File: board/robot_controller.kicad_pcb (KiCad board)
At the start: 2 copper layers, 325 parts, among them J101 +3.3V, J102 +24V, J103 GND, J104 JTAG-ARM, J105 Power, J106 FTDI-USB, J107 Industrial Inputs, J108 Industrial Outputs, J109 MCU-USB, J110 AUX-UART, J111 UEXT0, J112 UEXT1, J113 RGB LEDs, J201 Temp Probe, J2301 Stepper Motor, J2302 Limit-SW, J2401 Stepper Motor, J2402 Limit-SW, J2501 Stepper Motor, J2502 Limit-SW, J2601 Stepper Motor, J2602 Limit-SW, J301 Temp Probe, Q101 PNP, Q1501 NJT4031NT1G, Q1601 NJT4031NT1G, Q1701 NJT4031NT1G, Q1801 NJT4031NT1G, Q1901 NJT4031NT1G, Q2001 NJT4031NT1G, Q2101 NJT4031NT1G, Q2201 NJT4031NT1G, Q401 MMBT5962, Q402 MMBT5962, Q501 MMBT5962, Q502 MMBT5962, SW101 SW0, SW102 SW1, SW103 SW2, SW104 SW3, SW105 RESET, SW106 BOOT, U101 STM32F405-144, U102 FT232RL, U201 MAX6675, U2301 L6470, U2401 L6470, U2501 L6470, U2601 L6470, U301 MAX6675, U601 LMZ14201, X101 8MHZ

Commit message: Board pretty much done.
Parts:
- added G***: LOGO, components:roboteurs, F.Cu at (123.2, -139.1)
- added G***: LOGO, components:hypertriangle, F.Cu at (95.6, -139.1)
- added G***: LOGO, components:resistornetwork, F.Cu at (107.6, -139.1)
- J110: value AUX-UART -> AUX-USART6
- J201: value Temp Probe -> Temp 0
- J2301: value Stepper Motor -> Motor 0
- J2302: value Limit-SW -> Limit 0
- J2401: value Stepper Motor -> Motor 1
- J2402: value Limit-SW -> Limit 1
- J2501: value Stepper Motor -> Motor 2
- J2502: value Limit-SW -> Limit 2
- J2601: value Stepper Motor -> Motor 3
- J2602: value Limit-SW -> Limit 3
- J301: value Temp Probe -> Temp 1
- TP101: value STEPPERS_SCK -> STEP_SCK
- TP102: value STEPPERS_MOSI -> STEP_MOSI
- TP103: value STEPPERS_MISO -> STEP_MISO
- TP104: value STEPPER0-~CS -> STEP-~CS~0
- TP105: value STEPPER1-~CS -> STEP-~CS~1
- TP106: value STEPPER2-~CS -> STEP-~CS~2
- TP107: value STEPPER3-~CS -> STEP-~CS~3
- TP108: value STEPPER0_STCK -> STCK0
- TP109: value STEPPER1_STCK -> STCK1
- TP110: value STEPPER2_STCK -> STCK2
- TP111: value STEPPER3_STCK -> STCK3
- TP113: value STEPPERS_OSC_SYNC -> STEP_OSC_SYNC
- TP118: value USART1_RX -> RX
- TP119: value USART1_TX -> TX
- TP120: value USART1_CTS -> CTS
- TP121: value USART1_RTS -> RTS
- TP124: value TEMP_MISO -> MISO
- TP125: value TEMP_SCK -> SCK
- TP126: value TEMP0-~CS -> ~CS~0
- TP127: value TEMP1-~CS -> ~CS~1
- TP128: value SUPPLY_SENSE -> SUPPLY_SENSE (abs)
- TP129: value STEPPERS_SENSE -> STEPPERS_SENSE (var)
- moved C107 1.42 mm to (176.2, -135.6)
- moved C112 1.14 mm to (167.3, -140.0), turned to 90 degrees
- moved L101 1.14 mm to (165.7, -140.0), turned to 90 degrees
- moved C2311 0.90 mm to (109.2, -82.2)
- moved C2411 0.90 mm to (147.0, -82.2)
- moved C2511 0.90 mm to (184.8, -82.2)
- moved C2611 0.64 mm to (220.3, -82.2)
- moved R110 0.32 mm to (169.5, -141.0)
- moved R111 0.32 mm to (169.5, -139.4)
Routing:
- net GND: track 1025.7 -> 1036.0 mm, vias 301 -> 303
- net +24V: track 1237.9 -> 1241.5 mm
- net /MCU_RESET: track 76.1 -> 75.1 mm
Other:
- board text added: "3A Max Sinking"
- board text added: "Alexandru Stan & Andrew Rossignol"
- board text added: "I2C1"
- board text added: "I2C2"
- board text added: "MISO"
- board text added: "MOSI"
- board text added: "Max 40V"
- board text added: "Olimex UEXT"
- board text added: "RX"
- board text added: "Robot Controller"
- board text added: "SCK"
- board text added: "SCL"
- board text added: "SDA"
- board text added: "SPI1"
- board text added: "SPI1+HW ~CS~"
- board text added: "SPI2"
- board text added: "TX"
- board text added: "Temp-SPI3"
- board text added: "USART2"
- board text added: "USART3"
- board text added: "VCC"
- board text added: "v1.0 - Winter 2014"
- board text added: "~CS"

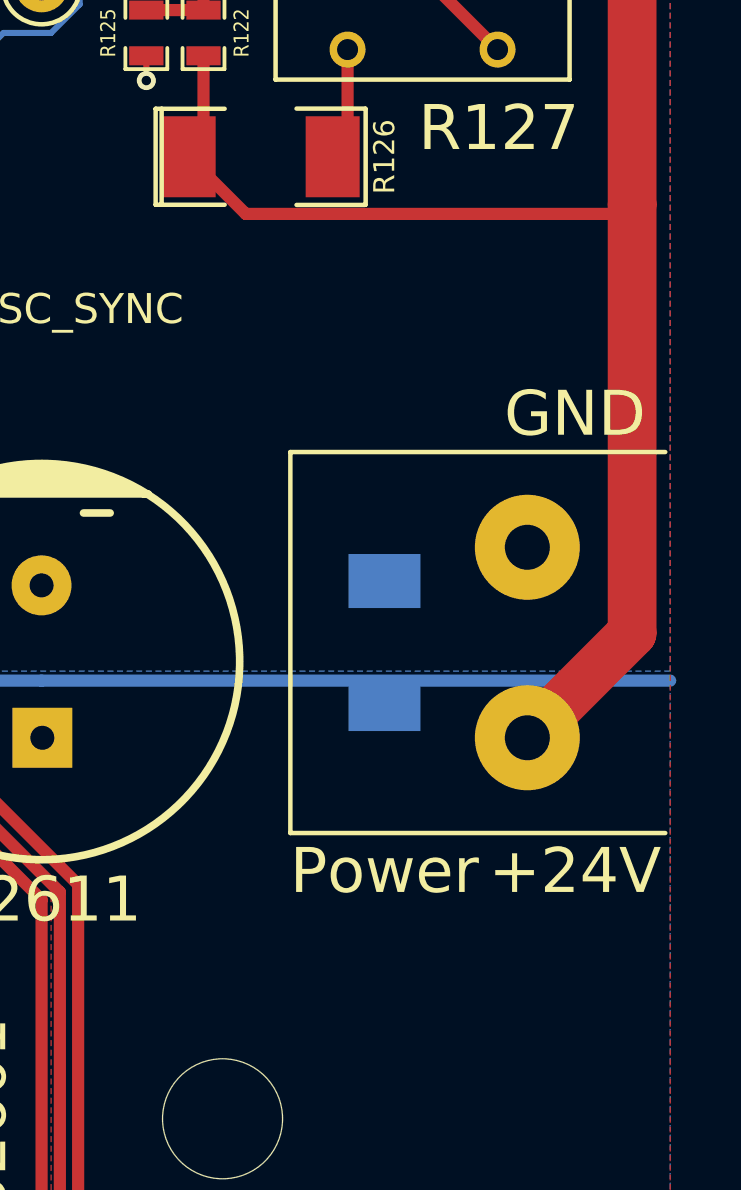
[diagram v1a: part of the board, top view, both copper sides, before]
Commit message: Fixed Main Power Footprint
Updated the footprint on the PCB layout and the track connected to it.
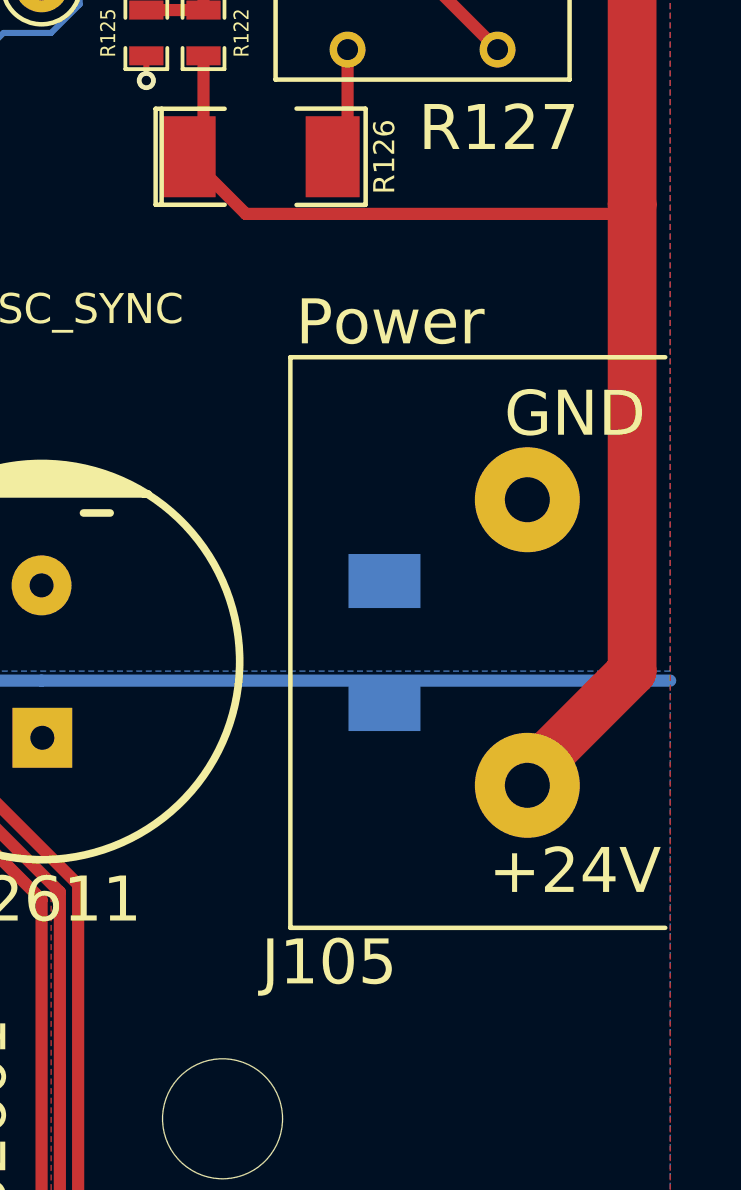
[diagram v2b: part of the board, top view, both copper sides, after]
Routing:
- net +24V: track 1241.5 -> 1242.8 mm
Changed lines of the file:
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@@
-(kicad_pcb (version 3) (host pcbnew "(2014-02-21 BZR 4712)-product")
+(kicad_pcb (version 3) (host pcbnew "(2014-01-30 BZR 4648)-product")
   (general
     (links 796)
@@
   (layers
     (15 F.Cu signal)
-    (0 B.Cu signal)
+    (0 B.Cu signal hide)
     (16 B.Adhes user)
     (17 F.Adhes user)
@@
       (net 119 GND))
   )
-  (module components:PWRSCONN_2 (layer F.Cu)
-    (at 236.5375 -82.8675 270)
-    (fp_text reference J105 (at 7.62 3.81 360) (layer F.SilkS) hide
-      (effects (font (size 1.5 1.5) (thickness 0.15)))
-    )
-    (fp_text value Power (at 7.62 4.7625 360) (layer F.SilkS)
-      (effects (font (size 1.5 1.5) (thickness 0.15)))
-    )
-    (fp_line (start -6.35 7.8994) (end 6.35 7.8994) (layer F.SilkS) (width 0.15))
-    (fp_line (start 6.35 7.8994) (end 6.35 -4.5974) (layer F.SilkS) (width 0.15))
-    (fp_line (start -6.35 7.8994) (end -6.35 -4.5974) (layer F.SilkS) (width 0.15))
-    (pad 1 thru_hole circle (at 3.175 0 270) (size 3.5 3.5) (drill 1.5) (layers *.Cu *.Mask F.SilkS)
-      (net 1 +24V))
-    (pad 2 thru_hole circle (at -3.175 0 270) (size 3.5 3.5) (drill 1.5) (layers *.Cu *.Mask F.SilkS)
-      (net 119 GND))
-  )
   (module components:SCONN_4 (layer F.Cu)
     (at 74.93 -83.5025 90)
@@
       (xy 2.134053 -1.938867) (xy 2.134053 -1.938867)) (layer F.SilkS) (width 0.01))
   )
+  (module components:PWRSCONN_2 (layer F.Cu)
+    (at 236.5375 -82.8675 270)
+    (fp_text reference J105 (at 10.668 6.604 360) (layer F.SilkS)
+      (effects (font (size 1.5 1.5) (thickness 0.15)))
+    )
+    (fp_text value Power (at -10.668 4.572 360) (layer F.SilkS)
+      (effects (font (size 1.5 1.5) (thickness 0.15)))
+    )
+    (fp_line (start -9.51 7.8994) (end 9.51 7.8994) (layer F.SilkS) (width 0.15))
+    (fp_line (start 9.51 7.8994) (end 9.51 -4.5974) (layer F.SilkS) (width 0.15))
+    (fp_line (start -9.51 7.8994) (end -9.51 -4.5974) (layer F.SilkS) (width 0.15))
+    (pad 1 thru_hole circle (at 4.76 0 270) (size 3.5 3.5) (drill 1.5) (layers *.Cu *.Mask F.SilkS)
+      (net 1 +24V))
+    (pad 2 thru_hole circle (at -4.76 0 270) (size 3.5 3.5) (drill 1.5) (layers *.Cu *.Mask F.SilkS)
+      (net 119 GND))
+  )
   (gr_text "Max 40V" (at 158.75 -168.5925) (layer F.SilkS)
     (effects (font (size 0.762 0.762) (thickness 0.127)))
@@
   (segment (start 236.2962 -139.065) (end 227.4062 -147.955) (width 1.6256) (layer F.Cu) (net 1))
   (segment (start 227.4062 -147.955) (end 224.155 -147.955) (width 1.6256) (layer F.Cu) (net 1))
-  (segment (start 236.5375 -79.6925) (end 240.03 -83.185) (width 1.6256) (layer F.Cu) (net 1))
-  (segment (start 240.03 -83.185) (end 240.03 -97.4725) (width 1.6256) (layer F.Cu) (net 1))
+  (segment (start 236.5375 -78.4225) (end 240.03 -81.915) (width 1.6256) (layer F.Cu) (net 1))
+  (segment (start 240.03 -81.915) (end 240.03 -97.4725) (width 1.6256) (layer F.Cu) (net 1))
   (segment (start 240.03 -97.4725) (end 240.03 -125.73) (width 1.6256) (layer F.Cu) (net 1))
   (segment (start 240.03 -125.73) (end 238.125 -127.635) (width 1.6256) (layer F.Cu) (net 1))

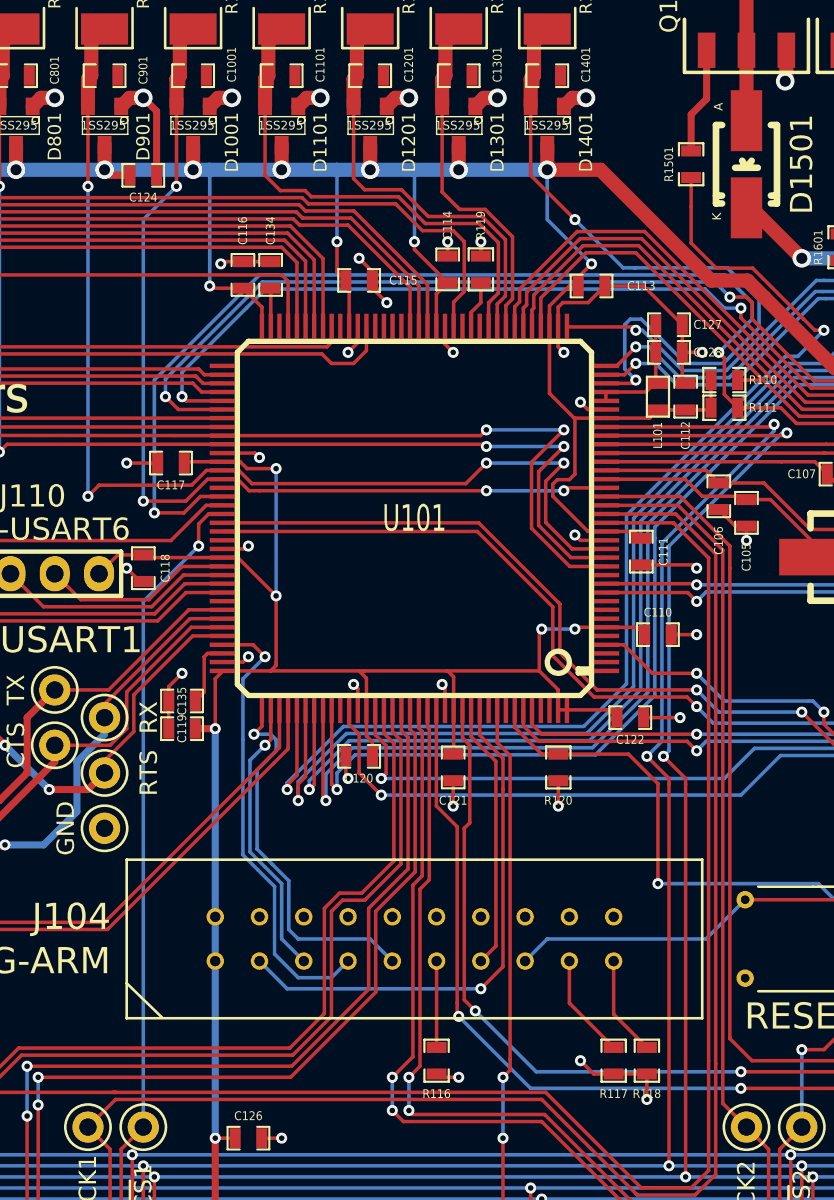
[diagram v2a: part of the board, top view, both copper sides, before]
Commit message: More silkscreen changes
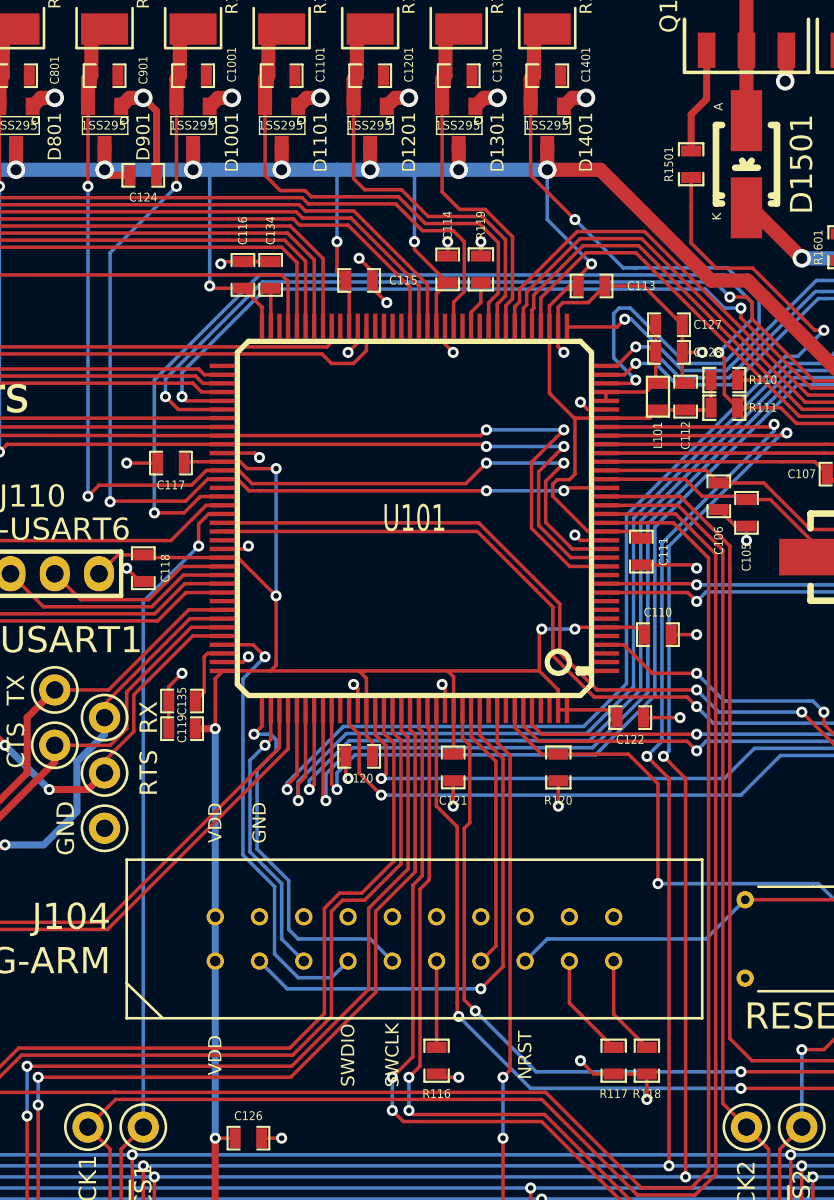
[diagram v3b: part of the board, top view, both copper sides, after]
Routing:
- net /Industrial Input 3/MCU_Input: track 55.7 -> 58.4 mm
- net /Industrial Input 7/MCU_Input: track 41.5 -> 43.3 mm
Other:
- board text added: "NRST"
- board text added: "SWCLK"
- board text added: "SWDIO"
- board text added: "VDD"

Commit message: moved board to fit in the page
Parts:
- moved C1001 208.6 mm to (94.6, 45.4)
- moved C106 208.6 mm to (124.8, 69.5)
- moved C108 208.6 mm to (186.7, 148.6)
- moved C109 208.6 mm to (187.3, 121.0)
- moved C1101 208.6 mm to (99.7, 45.4)
- moved C112 208.6 mm to (122.9, 63.8)
- moved C113 208.6 mm to (117.5, 57.5)
- moved C115 208.6 mm to (104.1, 57.1)
- moved C116 208.6 mm to (97.5, 56.8)
- moved C117 208.6 mm to (93.3, 67.6)
- moved C118 208.6 mm to (91.8, 73.7)
- moved C119 208.6 mm to (94.0, 82.9)
- moved C1201 208.6 mm to (104.8, 45.4)
- moved C121 208.6 mm to (109.5, 85.1)
- moved C122 208.6 mm to (119.7, 82.2)
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
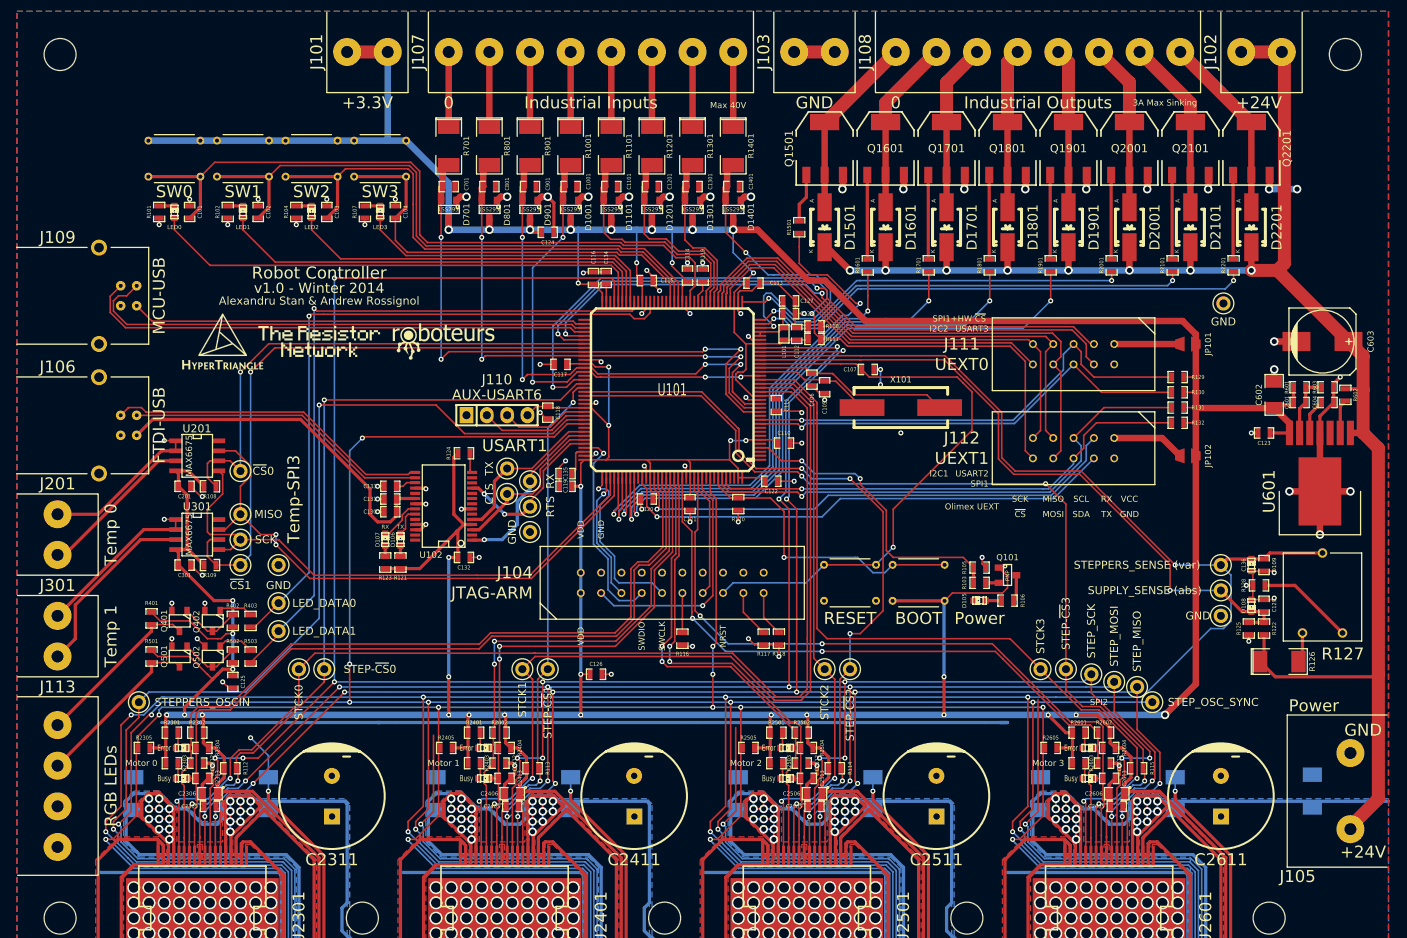
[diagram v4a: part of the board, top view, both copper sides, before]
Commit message: Fixed DRC with the new part changes
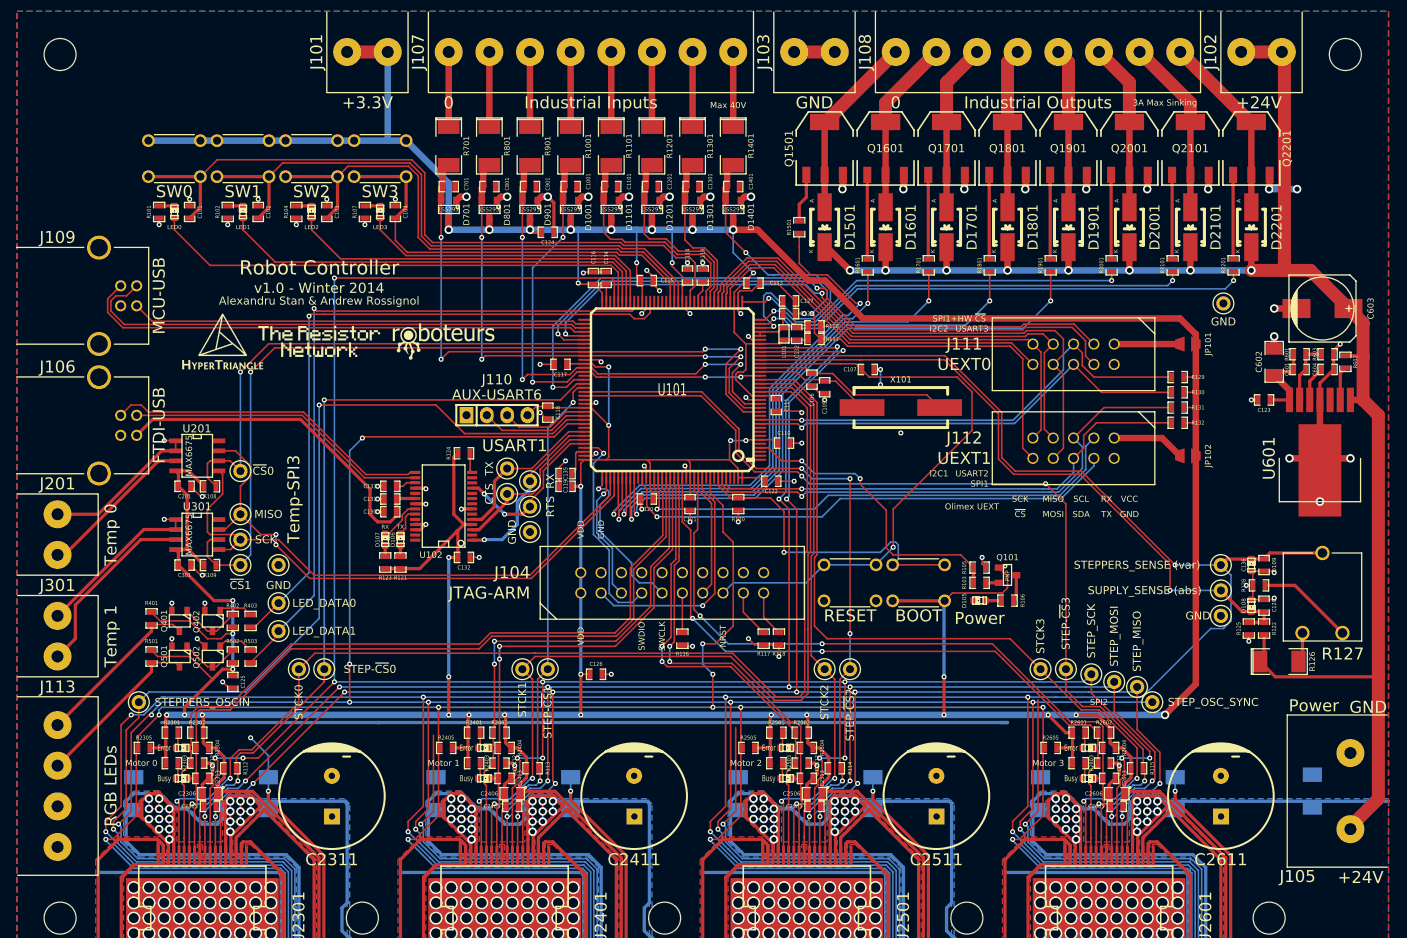
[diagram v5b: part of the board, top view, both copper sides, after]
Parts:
- moved C123 4.13 mm to (181.3, 72.1)
- moved C601 4.13 mm to (185.7, 68.3)
- moved C602 4.13 mm to (182.6, 67.3)
- moved C603 4.13 mm to (188.6, 60.6)
- moved C604 4.13 mm to (189.2, 68.3)
- moved R601 4.13 mm to (185.7, 66.4)
- moved R602 4.13 mm to (191.5, 67.3)
- moved R603 4.13 mm to (189.2, 66.4)
- moved U601 4.13 mm to (188.3, 79.4)
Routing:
- net +3.3V: track 982.2 -> 972.5 mm
- net /Stepper 2/~CS: track 95.6 -> 91.4 mm
- net /Stepper 0/~STBY/RST: track 434.9 -> 438.7 mm
- net /BOOT0: track 37.6 -> 39.9 mm
- net +24V: track 1242.8 -> 1244.9 mm
- net /JTCK/SWCLK: track 21.8 -> 20.3 mm
- net /SPI1_MOSI: track 66.3 -> 67.5 mm
- net /I2C1_SCL: track 65.3 -> 66.1 mm
- net /Stepper 0/~FLAG: track 98.7 -> 97.9 mm
- net /Stepper 0/~BUSY~/SYNC: track 98.9 -> 98.1 mm
- net /USB_DM: track 64.7 -> 65.3 mm
- net /USART2_RX: track 63.7 -> 64.3 mm
- net /I2C1_SDA: track 61.5 -> 62.1 mm
- net /USART2_TX: track 63.3 -> 63.8 mm
- net /Industrial Output 1/MCU_Pin: track 58.5 -> 58.0 mm

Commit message: Moved board in a cooler spot
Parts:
- moved C2603 10.0 mm to (155.6, 142.9)
- moved C2611 10.0 mm to (167.6, 115.9)
- moved C2614 10.0 mm to (151.8, 143.8)
- moved C601 10.0 mm to (177.5, 62.5)
- moved D108 10.0 mm to (171.4, 92.1)
- moved D2201 10.0 mm to (171.4, 44.8)
- moved J2601 10.0 mm to (153.7, 155.3)
- moved JP101 10.0 mm to (163.5, 59.4)
- moved JP102 10.0 mm to (163.5, 73.3)
- moved MH 10.0 mm to (135.9, 131.1)
- moved Q2201 10.0 mm to (171.4, 34.9)
- moved R601 10.0 mm to (177.5, 60.6)
- moved SW106 10.0 mm to (129.9, 89.2)
- moved TP115 10.0 mm to (167.6, 93.3)
- moved TP128 10.0 mm to (167.6, 90.2)
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
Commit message: More silkscreen changes, more track fiddling.
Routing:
- net /Stepper 3/OSCOUT: track 69.4 -> 0.00 mm, vias 2 -> 0
- net /Stepper 2/OSCOUT: track 65.9 -> 0.00 mm, vias 2 -> 0
- net /Stepper 1/OSCOUT: track 64.9 -> 0.00 mm, vias 2 -> 0
- net +3.3V: track 972.5 -> 982.8 mm
- net GND: track 1036.0 -> 1040.9 mm, vias 303 -> 304
- net /LED_PWR: track 37.9 -> 38.7 mm
- net /MCU_RESET: track 75.1 -> 74.6 mm
- net (no net): vias 1 -> 0
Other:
- board outline added: 171.4 x 142.6 mm
- rule pad_to_mask_clearance: 0.2 -> 0.1016
- board text added: "1A"
- board text added: "1B"
- board text added: "2A"
- board text added: "2B"
